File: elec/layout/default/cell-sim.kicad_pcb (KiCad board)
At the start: 2 copper layers, 225.7 x 100.8 mm, 0 parts

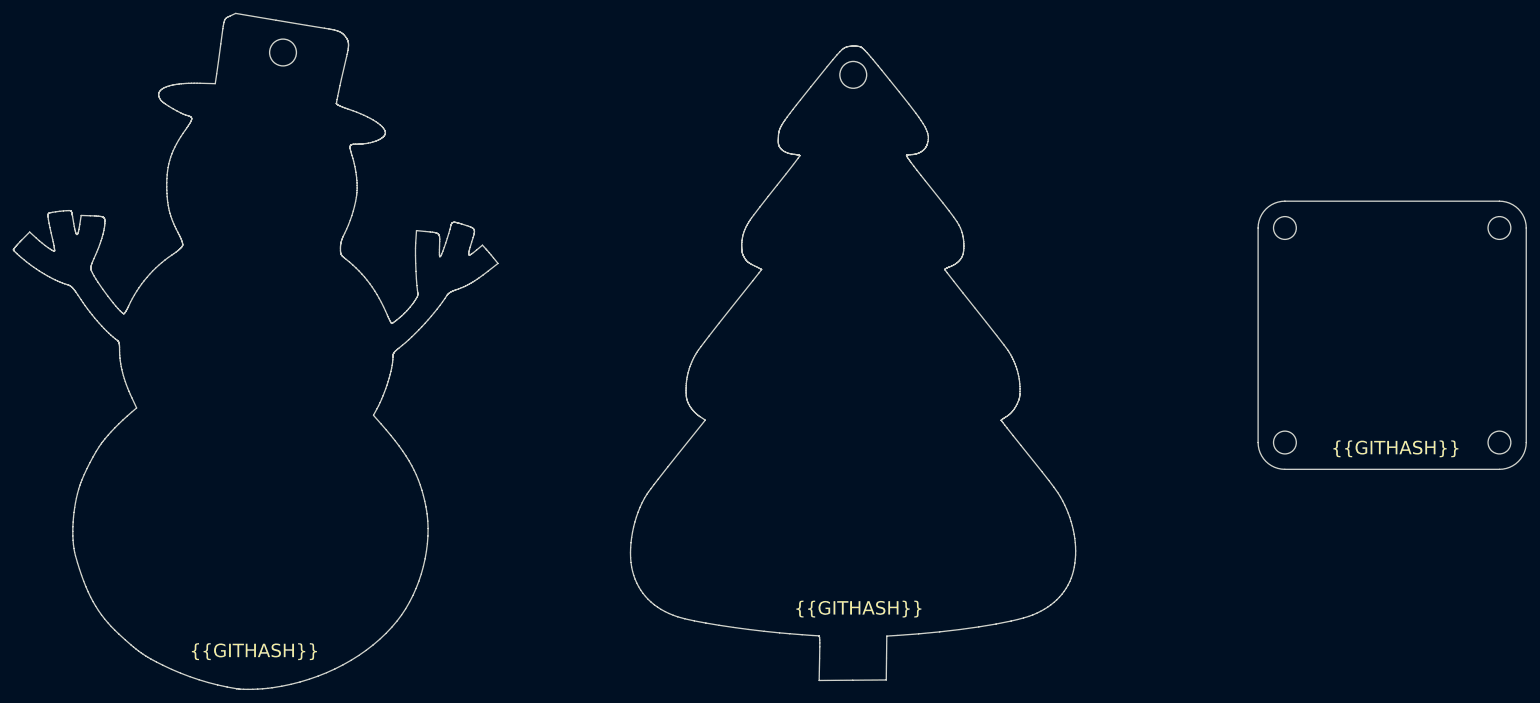
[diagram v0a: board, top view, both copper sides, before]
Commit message: merge firmware and layout from BMS project
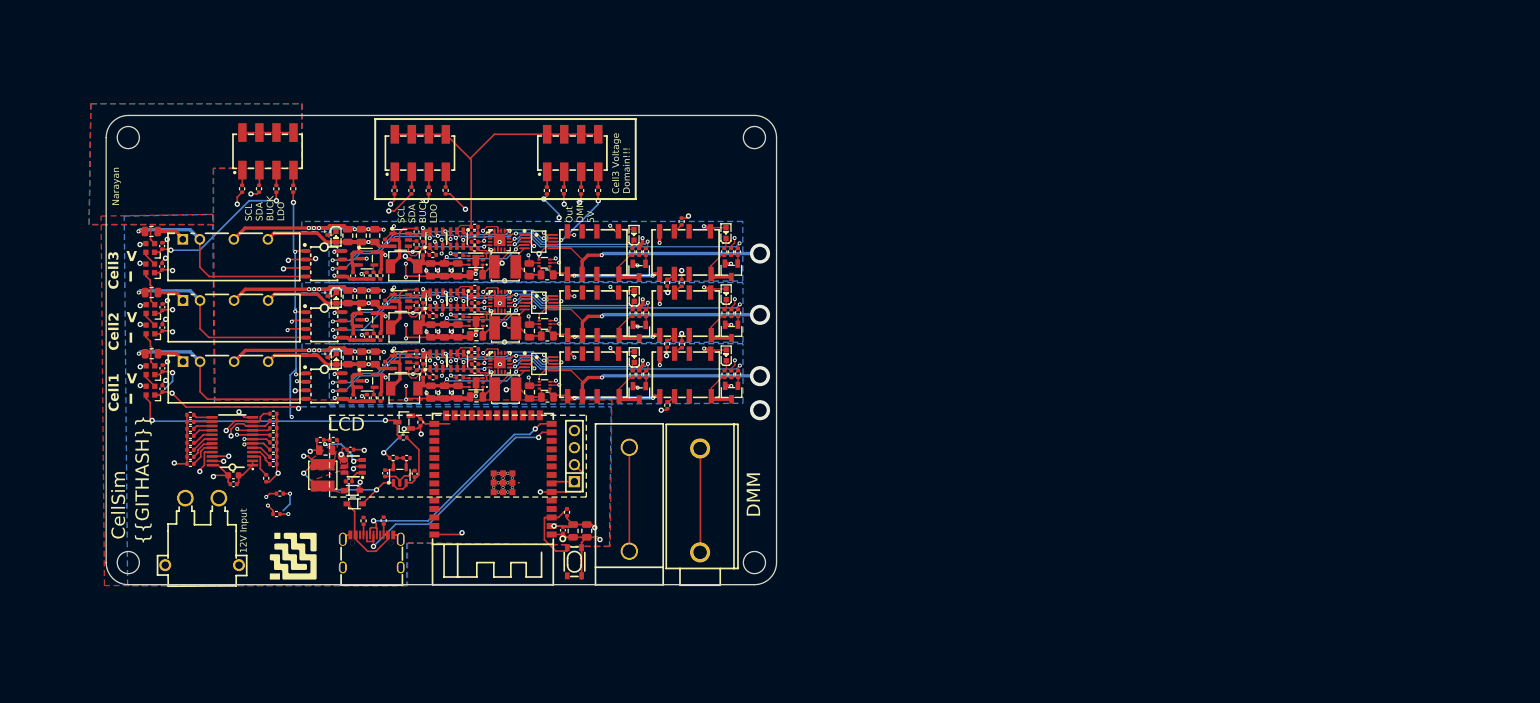
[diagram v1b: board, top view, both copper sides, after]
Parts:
- added C1: 16V 100nF X7R ±10% 0402 Multilayer Ceramic Capacitors MLCC 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, lib:C0402, F.Cu at (117.9, 126.9)
- added C10: 25V 1uF X5R ±10% 0402 Multilayer Ceramic Capacitors MLCC - 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, lib:C0402, F.Cu at (91.4, 118.4)
- added C11: 50V 2.2uF X5R ±10% 0805 Multilayer Ceramic Capacitors MLCC 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, lib:C0805, F.Cu at (56.6, 100.5)
- added C12: 25V 10uF X5R ±10% 0805 Multilayer Ceramic Capacitors MLCC -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, lib:C0805, F.Cu at (85.9, 101.2)
- added C13: 25V 10uF X5R ±10% 0805 Multilayer Ceramic Capacitors MLCC -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, lib:C0805, F.Cu at (89.9, 101.2)
- added C14: 25V 10uF X5R ±10% 0805 Multilayer Ceramic Capacitors MLCC -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, lib:C0805, F.Cu at (87.9, 101.2)
- added C15: 16V 100nF X7R ±10% 0402 Multilayer Ceramic Capacitors MLCC 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, lib:C0402, F.Cu at (91.4, 102.2)
- added C16: 25V 10uF X5R ±10% 0805 Multilayer Ceramic Capacitors MLCC -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, lib:C0805, F.Cu at (100.3, 106.3)
- added C17: 25V 10uF X5R ±10% 0805 Multilayer Ceramic Capacitors MLCC -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, lib:C0805, F.Cu at (102.3, 106.3)
- added C18: 25V 10uF X5R ±10% 0805 Multilayer Ceramic Capacitors MLCC -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, lib:C0805, F.Cu at (98.2, 106.3)
- added C19: 16V 100nF X7R ±10% 0402 Multilayer Ceramic Capacitors MLCC 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, lib:C0402, F.Cu at (96.1, 100.6)
- added C2: 25V 10uF X5R ±10% 0805 Multilayer Ceramic Capacitors MLCC -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, lib:C0805, F.Cu at (119.4, 127.0)
- added C20: 25V 1uF X5R ±10% 0402 Multilayer Ceramic Capacitors MLCC - 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, lib:C0402, F.Cu at (104.8, 102.1)
- added C21: 25V 10uF X5R ±10% 0805 Multilayer Ceramic Capacitors MLCC -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, lib:C0805, F.Cu at (105.0, 107.0)
- added C22: 25V 10uF X5R ±10% 0805 Multilayer Ceramic Capacitors MLCC -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, lib:C0805, F.Cu at (112.9, 106.3)
- added C23: 16V 100nF X7R ±10% 0402 Multilayer Ceramic Capacitors MLCC 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, lib:C0402, F.Cu at (58.2, 102.7)
- added C24: 16V 100nF X7R ±10% 0402 Multilayer Ceramic Capacitors MLCC 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, lib:C0402, F.Cu at (58.2, 105.8)
- added C25: 25V 1uF X5R ±10% 0402 Multilayer Ceramic Capacitors MLCC - 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, lib:C0402, F.Cu at (86.7, 107.1)
- added C26: 25V 1uF X5R ±10% 0402 Multilayer Ceramic Capacitors MLCC - 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, lib:C0402, F.Cu at (88.7, 107.1)
- added C27: 50V 2.2uF X5R ±10% 0805 Multilayer Ceramic Capacitors MLCC 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, lib:C0805, F.Cu at (56.6, 91.4)
- added C28: 25V 10uF X5R ±10% 0805 Multilayer Ceramic Capacitors MLCC -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, lib:C0805, F.Cu at (85.9, 92.0)
- added C29: 25V 10uF X5R ±10% 0805 Multilayer Ceramic Capacitors MLCC -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, lib:C0805, F.Cu at (89.9, 92.0)
- added C3: 25V 10uF X5R ±10% 0805 Multilayer Ceramic Capacitors MLCC -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, lib:C0805, F.Cu at (121.5, 127.0)
- added C30: 25V 10uF X5R ±10% 0805 Multilayer Ceramic Capacitors MLCC -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, lib:C0805, F.Cu at (87.9, 92.1)
- added C31: 16V 100nF X7R ±10% 0402 Multilayer Ceramic Capacitors MLCC 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, lib:C0402, F.Cu at (91.4, 93.1)
- added C32: 25V 10uF X5R ±10% 0805 Multilayer Ceramic Capacitors MLCC -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, lib:C0805, F.Cu at (100.3, 97.2)
- added C33: 25V 10uF X5R ±10% 0805 Multilayer Ceramic Capacitors MLCC -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, lib:C0805, F.Cu at (102.3, 97.2)
- added C34: 25V 10uF X5R ±10% 0805 Multilayer Ceramic Capacitors MLCC -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, lib:C0805, F.Cu at (98.2, 97.2)
- added C35: 16V 100nF X7R ±10% 0402 Multilayer Ceramic Capacitors MLCC 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, lib:C0402, F.Cu at (96.1, 91.5)
- added C36: 25V 1uF X5R ±10% 0402 Multilayer Ceramic Capacitors MLCC - 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, lib:C0402, F.Cu at (104.8, 93.0)
- added C37: 25V 10uF X5R ±10% 0805 Multilayer Ceramic Capacitors MLCC -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, lib:C0805, F.Cu at (105.0, 97.9)
- added C38: 25V 10uF X5R ±10% 0805 Multilayer Ceramic Capacitors MLCC -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, lib:C0805, F.Cu at (112.9, 97.2)
- added C39: 16V 100nF X7R ±10% 0402 Multilayer Ceramic Capacitors MLCC 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, lib:C0402, F.Cu at (58.2, 93.6)
- added C4: 16V 100nF X7R ±10% 0402 Multilayer Ceramic Capacitors MLCC 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, lib:C0402, F.Cu at (68.8, 120.0)
- added C40: 16V 100nF X7R ±10% 0402 Multilayer Ceramic Capacitors MLCC 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, lib:C0402, F.Cu at (58.2, 96.6)
- added C41: 25V 1uF X5R ±10% 0402 Multilayer Ceramic Capacitors MLCC - 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, lib:C0402, F.Cu at (86.6, 98.0)
- added C42: 25V 1uF X5R ±10% 0402 Multilayer Ceramic Capacitors MLCC - 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, lib:C0402, F.Cu at (88.7, 98.0)
- added C43: 50V 2.2uF X5R ±10% 0805 Multilayer Ceramic Capacitors MLCC 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, lib:C0805, F.Cu at (56.5, 82.3)
- added C44: 25V 10uF X5R ±10% 0805 Multilayer Ceramic Capacitors MLCC -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, lib:C0805, F.Cu at (85.8, 82.9)
- added C45: 25V 10uF X5R ±10% 0805 Multilayer Ceramic Capacitors MLCC -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, lib:C0805, F.Cu at (89.9, 82.9)
- added C46: 25V 10uF X5R ±10% 0805 Multilayer Ceramic Capacitors MLCC -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, lib:C0805, F.Cu at (87.8, 82.9)
- added C47: 16V 100nF X7R ±10% 0402 Multilayer Ceramic Capacitors MLCC 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, lib:C0402, F.Cu at (91.4, 84.0)
- added C48: 25V 10uF X5R ±10% 0805 Multilayer Ceramic Capacitors MLCC -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, lib:C0805, F.Cu at (100.2, 88.0)
- added C49: 25V 10uF X5R ±10% 0805 Multilayer Ceramic Capacitors MLCC -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, lib:C0805, F.Cu at (102.2, 88.0)
- added C5: 16V 2.2uF X5R ±10% 0603 Multilayer Ceramic Capacitors MLCC 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, lib:C0603, F.Cu at (68.8, 118.7)
- added C50: 25V 10uF X5R ±10% 0805 Multilayer Ceramic Capacitors MLCC -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, lib:C0805, F.Cu at (98.2, 88.0)
- added C51: 16V 100nF X7R ±10% 0402 Multilayer Ceramic Capacitors MLCC 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, lib:C0402, F.Cu at (96.1, 82.3)
- added C52: 25V 1uF X5R ±10% 0402 Multilayer Ceramic Capacitors MLCC - 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, lib:C0402, F.Cu at (104.8, 83.8)
- added C53: 25V 10uF X5R ±10% 0805 Multilayer Ceramic Capacitors MLCC -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, lib:C0805, F.Cu at (105.0, 88.8)
- added C54: 25V 10uF X5R ±10% 0805 Multilayer Ceramic Capacitors MLCC -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, lib:C0805, F.Cu at (112.9, 88.0)
- added C55: 16V 100nF X7R ±10% 0402 Multilayer Ceramic Capacitors MLCC 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, lib:C0402, F.Cu at (58.1, 84.5)
- added C56: 16V 100nF X7R ±10% 0402 Multilayer Ceramic Capacitors MLCC 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, lib:C0402, F.Cu at (58.1, 87.5)
- added C57: 25V 1uF X5R ±10% 0402 Multilayer Ceramic Capacitors MLCC - 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, lib:C0402, F.Cu at (86.6, 88.9)
- added C58: 25V 1uF X5R ±10% 0402 Multilayer Ceramic Capacitors MLCC - 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, lib:C0402, F.Cu at (88.6, 88.9)
- added C6: 6.3V 10uF X5R ±20% 0402 Multilayer Ceramic Capacitors MLCC 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, lib:C0402, F.Cu at (86.2, 114.9)
- added C7: 25V 10uF X5R ±10% 0805 Multilayer Ceramic Capacitors MLCC -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, lib:C0805, F.Cu at (82.5, 114.9)
- added C8: 16V 100nF X7R ±10% 0402 Multilayer Ceramic Capacitors MLCC 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, lib:C0402, F.Cu at (86.0, 119.6)
- added C9: 25V 1uF X5R ±10% 0402 Multilayer Ceramic Capacitors MLCC - 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, lib:C0402, F.Cu at (95.8, 118.5)
- added DS1: , lib:SOD-323_L1.8-W1.3-LS2.5-RD, F.Cu at (86.4, 120.9)
- added DS2: , lib:SOD-323_L1.8-W1.3-LS2.5-RD, F.Cu at (86.9, 122.9)
- added J1: , lib:CONN-TH_XT30PW-M, F.Cu at (64.1, 127.1)
- added L1: , lib:IND-SMD_L4.0-W4.0, F.Cu at (82.1, 118.7)
- added L2: , lib:IND-SMD_L4.4-W4.2, F.Cu at (94.3, 105.7)
- added L3: 100uH, lib:IND-SMD_L4.0-W4.0, F.Cu at (109.3, 105.8)
- added L4: , lib:IND-SMD_L4.4-W4.2, F.Cu at (94.3, 96.6)
- added L5: 100uH, lib:IND-SMD_L4.0-W4.0, F.Cu at (109.3, 96.7)
- added L6: , lib:IND-SMD_L4.4-W4.2, F.Cu at (94.2, 87.5)
- added L7: 100uH, lib:IND-SMD_L4.0-W4.0, F.Cu at (109.3, 87.6)
- added LED1: , lib:LED0603-RD, F.Cu at (84.1, 101.3)
- added LED2: , lib:LED0603-RD, F.Cu at (128.6, 101.0)
- added LED3: , lib:LED0603-RD, F.Cu at (142.3, 100.8)
- added LED4: , lib:LED0603-RD, F.Cu at (84.1, 92.2)
- added LED5: , lib:LED0603-RD, F.Cu at (128.6, 91.9)
- added LED6: , lib:LED0603-RD, F.Cu at (142.3, 91.7)
- added LED7: , lib:LED0603-RD, F.Cu at (84.1, 83.1)
- added LED8: , lib:LED0603-RD, F.Cu at (128.5, 82.8)
- added LED9: , lib:LED0603-RD, F.Cu at (142.2, 82.5)
- added Q1: , lib:SOT-23-3_L2.9-W1.3-P1.90-LS2.4-BR, F.Cu at (129.3, 106.4)
- added Q2: , lib:SOT-23-3_L2.9-W1.3-P1.90-LS2.4-BR, F.Cu at (143.1, 106.3)
- added Q3: , lib:SOT-23-3_L2.9-W1.3-P1.90-LS2.4-BR, F.Cu at (129.3, 97.3)
- added Q4: , lib:SOT-23-3_L2.9-W1.3-P1.90-LS2.4-BR, F.Cu at (143.1, 97.2)
- added Q5: , lib:SOT-23-3_L2.9-W1.3-P1.90-LS2.4-BR, F.Cu at (129.3, 88.1)
- added Q6: , lib:SOT-23-3_L2.9-W1.3-P1.90-LS2.4-BR, F.Cu at (143.0, 88.1)
- added R1: 62.5mW Thick Film Resistors 50V ±100ppm/℃ ±1% 10kΩ 0402 Chi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, lib:R0402, F.Cu at (118.5, 124.2)
- added R10: 62.5mW Thick Film Resistors 50V ±100ppm/℃ ±1% 10kΩ 0402 Chi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, lib:R0402, F.Cu at (74.7, 112.7)
- added R100: 62.5mW Thick Film Resistors 50V ±100ppm/℃ ±1% 1kΩ 0402 Chip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, lib:R0402, F.Cu at (123.2, 76.2)
- added R11: 62.5mW Thick Film Resistors 50V ±100ppm/℃ ±1% 10kΩ 0402 Chi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, lib:R0402, F.Cu at (74.7, 109.5)
- added R12: 62.5mW Thick Film Resistors 50V ±100ppm/℃ ±1% 10kΩ 0402 Chi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, lib:R0402, F.Cu at (74.7, 110.6)
- added R13: 62.5mW Thick Film Resistors 50V ±100ppm/℃ ±1% 10kΩ 0402 Chi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, lib:R0402, F.Cu at (62.3, 110.7)
- added R14: 62.5mW Thick Film Resistors 50V ±100ppm/℃ ±1% 10kΩ 0402 Chi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, lib:R0402, F.Cu at (62.3, 109.7)
- added R15: 62.5mW Thick Film Resistors 50V ±100ppm/℃ ±1% 10kΩ 0402 Chi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, lib:R0402, F.Cu at (62.3, 112.8)
- added R16: 62.5mW Thick Film Resistors 50V ±100ppm/℃ ±1% 10kΩ 0402 Chi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, lib:R0402, F.Cu at (62.3, 111.8)
- added R17: 62.5mW Thick Film Resistors 50V ±100ppm/℃ ±1% 10kΩ 0402 Chi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, lib:R0402, F.Cu at (62.3, 114.9)
- added R18: 62.5mW Thick Film Resistors 50V ±100ppm/℃ ±1% 10kΩ 0402 Chi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, lib:R0402, F.Cu at (62.3, 113.8)
- added R19: 62.5mW Thick Film Resistors 50V ±100ppm/℃ ±1% 10kΩ 0402 Chi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, lib:R0402, F.Cu at (62.3, 117.0)
- added R2: 62.5mW Thick Film Resistors 50V ±100ppm/℃ ±1% 4.7kΩ 0402 Ch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, lib:R0402, F.Cu at (88.2, 125.5)
- added R20: 62.5mW Thick Film Resistors 50V ±100ppm/℃ ±1% 10kΩ 0402 Chi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, lib:R0402, F.Cu at (62.3, 115.9)
- added R21: 62.5mW Thick Film Resistors 50V ±100ppm/℃ ±1% 2.2kΩ 0402 Ch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, lib:R0402, F.Cu at (75.2, 124.5)
- added R22: 62.5mW Thick Film Resistors 50V ±100ppm/℃ ±1% 2.2kΩ 0402 Ch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, lib:R0402, F.Cu at (75.7, 121.4)
- added R23: 62.5mW Thick Film Resistors 50V ±1% ±200ppm/℃ 22.6kΩ 0402 C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, lib:R0402, F.Cu at (83.7, 113.4)
- added R24: 62.5mW Thick Film Resistors 50V ±1% ±100ppm/℃ 4.12kΩ 0402 C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, lib:R0402, F.Cu at (81.7, 113.4)
- added R25: 62.5mW Thick Film Resistors 50V ±100ppm/℃ ±1% 17.4kΩ 0402 C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, lib:R0402, F.Cu at (92.6, 116.1)
- added R26: 62.5mW Thick Film Resistors 50V ±100ppm/℃ ±1% 10.2kΩ 0402 C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, lib:R0402, F.Cu at (94.6, 116.1)
- added R27: 62.5mW Thick Film Resistors 50V ±100ppm/℃ ±1% 10kΩ 0402 Chi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, lib:R0402, F.Cu at (96.7, 110.8)
- added R28: 62.5mW Thick Film Resistors 50V ±100ppm/℃ ±1% 10kΩ 0402 Chi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, lib:R0402, F.Cu at (94.1, 113.0)
- added R29: 62.5mW Thick Film Resistors 50V ±100ppm/℃ ±1% 21kΩ 0402 Chi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, lib:R0402, F.Cu at (82.8, 100.6)
- added R3: 62.5mW Thick Film Resistors 50V ±100ppm/℃ ±1% 4.7kΩ 0402 Ch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, lib:R0402, F.Cu at (91.2, 125.4)
- added R30: 62.5mW Thick Film Resistors 50V ±100ppm/℃ ±1% 24kΩ 0402 Chi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, lib:R0402, F.Cu at (98.5, 104.0)
- added R31: 62.5mW Thick Film Resistors 50V ±100ppm/℃ ±1% 37.4kΩ 0402 C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, lib:R0402, F.Cu at (97.1, 103.6)
- added R32: 62.5mW Thick Film Resistors 50V ±100ppm/℃ ±1% 10kΩ 0402 Chi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, lib:R0402, F.Cu at (97.1, 101.5)
- added R33: 62.5mW Thick Film Resistors 50V ±100ppm/℃ ±1% 10kΩ 0402 Chi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, lib:R0402, F.Cu at (96.1, 102.5)
- added R34: 62.5mW Thick Film Resistors 50V ±100ppm/℃ ±1% 43kΩ 0402 Chi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, lib:R0402, F.Cu at (104.8, 100.9)
- added R35: 62.5mW Thick Film Resistors 50V ±100ppm/℃ ±1% 59kΩ 0402 Chi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, lib:R0402, F.Cu at (104.8, 103.1)
- added R36: 62.5mW Thick Film Resistors 50V ±100ppm/℃ ±1% 10kΩ 0402 Chi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, lib:R0402, F.Cu at (104.8, 99.9)
- added R37: 62.5mW Thick Film Resistors 50V ±100ppm/℃ ±1% 10kΩ 0402 Chi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, lib:R0402, F.Cu at (102.5, 104.1)
- added R38: 125mW Thick Film Resistors ±600ppm/℃ ±1% 110mΩ 0805 Chip Re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, lib:R0805, F.Cu at (115.6, 107.0)
- added R39: 62.5mW Thick Film Resistors 50V ±100ppm/℃ ±1% 21kΩ 0402 Chi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, lib:R0402, F.Cu at (128.3, 103.6)
- added R4: 62.5mW Thick Film Resistors 50V ±100ppm/℃ ±1% 10kΩ 0402 Chi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, lib:R0402, F.Cu at (73.7, 119.1)
- added R40: 62.5mW Thick Film Resistors 50V ±100ppm/℃ ±1% 10kΩ 0402 Chi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, lib:R0402, F.Cu at (130.3, 103.6)
- added R41: 62.5mW Thick Film Resistors 50V ±100ppm/℃ ±1% 1kΩ 0402 Chip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, lib:R0402, F.Cu at (129.3, 103.6)
- added R42: 62.5mW Thick Film Resistors 50V ±100ppm/℃ ±1% 21kΩ 0402 Chi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, lib:R0402, F.Cu at (142.0, 103.6)
- added R43: 62.5mW Thick Film Resistors 50V ±100ppm/℃ ±1% 10kΩ 0402 Chi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, lib:R0402, F.Cu at (144.1, 103.6)
- added R44: 62.5mW Thick Film Resistors 50V ±100ppm/℃ ±1% 1kΩ 0402 Chip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, lib:R0402, F.Cu at (143.0, 103.6)
- added R45: 62.5mW Thick Film Resistors 50V ±100ppm/℃ ±1% 11.5kΩ 0402 C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, lib:R0402, F.Cu at (90.7, 107.1)
- added R46: 62.5mW Thick Film Resistors 50V ±100ppm/℃ ±1% 6.2kΩ 0402 Ch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, lib:R0402, F.Cu at (89.7, 107.1)
- added R47: 62.5mW Thick Film Resistors 50V ±100ppm/℃ ±1% 10kΩ 0402 Chi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, lib:R0402, F.Cu at (133.5, 108.2)
- added R48: 62.5mW Thick Film Resistors 50V ±100ppm/℃ ±1% 10kΩ 0402 Chi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, lib:R0402, F.Cu at (135.7, 99.1)
- added R49: 62.5mW Thick Film Resistors 50V ±100ppm/℃ ±1% 21kΩ 0402 Chi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, lib:R0402, F.Cu at (82.8, 91.4)
- added R5: 62.5mW Thick Film Resistors 50V ±100ppm/℃ ±1% 10kΩ 0402 Chi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, lib:R0402, F.Cu at (74.7, 115.9)
- added R50: 62.5mW Thick Film Resistors 50V ±100ppm/℃ ±1% 24kΩ 0402 Chi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, lib:R0402, F.Cu at (98.5, 94.9)
- added R51: 62.5mW Thick Film Resistors 50V ±100ppm/℃ ±1% 37.4kΩ 0402 C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, lib:R0402, F.Cu at (97.1, 94.5)
- added R52: 62.5mW Thick Film Resistors 50V ±100ppm/℃ ±1% 10kΩ 0402 Chi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, lib:R0402, F.Cu at (97.1, 92.4)
- added R53: 62.5mW Thick Film Resistors 50V ±100ppm/℃ ±1% 10kΩ 0402 Chi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, lib:R0402, F.Cu at (96.1, 93.4)
- added R54: 62.5mW Thick Film Resistors 50V ±100ppm/℃ ±1% 43kΩ 0402 Chi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, lib:R0402, F.Cu at (104.8, 91.8)
- added R55: 62.5mW Thick Film Resistors 50V ±100ppm/℃ ±1% 59kΩ 0402 Chi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, lib:R0402, F.Cu at (104.8, 94.0)
- added R56: 62.5mW Thick Film Resistors 50V ±100ppm/℃ ±1% 10kΩ 0402 Chi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, lib:R0402, F.Cu at (104.8, 90.7)
- added R57: 62.5mW Thick Film Resistors 50V ±100ppm/℃ ±1% 10kΩ 0402 Chi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, lib:R0402, F.Cu at (102.5, 95.0)
- added R58: 125mW Thick Film Resistors ±600ppm/℃ ±1% 110mΩ 0805 Chip Re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, lib:R0805, F.Cu at (115.6, 97.9)
- added R59: 62.5mW Thick Film Resistors 50V ±100ppm/℃ ±1% 21kΩ 0402 Chi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, lib:R0402, F.Cu at (128.3, 94.5)
- added R6: 62.5mW Thick Film Resistors 50V ±100ppm/℃ ±1% 10kΩ 0402 Chi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, lib:R0402, F.Cu at (74.7, 117.0)
- added R60: 62.5mW Thick Film Resistors 50V ±100ppm/℃ ±1% 10kΩ 0402 Chi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, lib:R0402, F.Cu at (130.3, 94.5)
- added R61: 62.5mW Thick Film Resistors 50V ±100ppm/℃ ±1% 1kΩ 0402 Chip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, lib:R0402, F.Cu at (129.3, 94.5)
- added R62: 62.5mW Thick Film Resistors 50V ±100ppm/℃ ±1% 21kΩ 0402 Chi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, lib:R0402, F.Cu at (142.0, 94.5)
- added R63: 62.5mW Thick Film Resistors 50V ±100ppm/℃ ±1% 10kΩ 0402 Chi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, lib:R0402, F.Cu at (144.1, 94.5)
- added R64: 62.5mW Thick Film Resistors 50V ±100ppm/℃ ±1% 1kΩ 0402 Chip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, lib:R0402, F.Cu at (143.0, 94.5)
- added R65: 62.5mW Thick Film Resistors 50V ±100ppm/℃ ±1% 11.5kΩ 0402 C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, lib:R0402, F.Cu at (90.7, 98.0)
- added R66: 62.5mW Thick Film Resistors 50V ±100ppm/℃ ±1% 6.2kΩ 0402 Ch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, lib:R0402, F.Cu at (89.7, 98.0)
- added R67: 62.5mW Thick Film Resistors 50V ±100ppm/℃ ±1% 10kΩ 0402 Chi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, lib:R0402, F.Cu at (133.5, 99.1)
- added R68: 62.5mW Thick Film Resistors 50V ±100ppm/℃ ±1% 10kΩ 0402 Chi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, lib:R0402, F.Cu at (135.6, 90.0)
- added R69: 62.5mW Thick Film Resistors 50V ±100ppm/℃ ±1% 21kΩ 0402 Chi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, lib:R0402, F.Cu at (82.8, 82.3)
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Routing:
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- added copper zone on F.Cu, net buck.ic-sw
- added copper zone on B.Cu, net cell1-gnd
- added copper zone on In2.Cu, net cell1-gnd
- added copper zone on In1.Cu, net cell1-vcc-2
- added copper zone on B.Cu, net cell2-gnd-1
- added copper zone on In2.Cu, net cell2-gnd-1
- added copper zone on In1.Cu, net cell2-vcc-2
- added copper zone on In1.Cu, net cell3-vcc-2
- added copper zone on B.Cu, net gnd
- added copper zone on F.Cu, net gnd
- added copper zone on In2.Cu, net gnd
- added copper zone on F.Cu, net vcc
- added copper zone on F.Cu, net vcc-2
- added copper zone on B.Cu, net vcc-3
- added copper zone on In1.Cu, net vcc-3
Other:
- board size 225.7 x 100.8 mm -> 100 x 70 mm
- copper layers 2 -> 4
- board text added: "12V Input"
- board text added: "Cell1"
- board text added: "Cell2"
- board text added: "Cell3"
- board text added: "Cell3 Voltage Domain!!!"
- board text added: "CellSim"
- board text added: "DMM"
- board text added: "I"
- board text added: "I Out DMM 5V"
- board text added: "LCD"
- board text added: "Narayan"
- board text added: "SCL SDA BUCK LDO"
- board text added: "V"

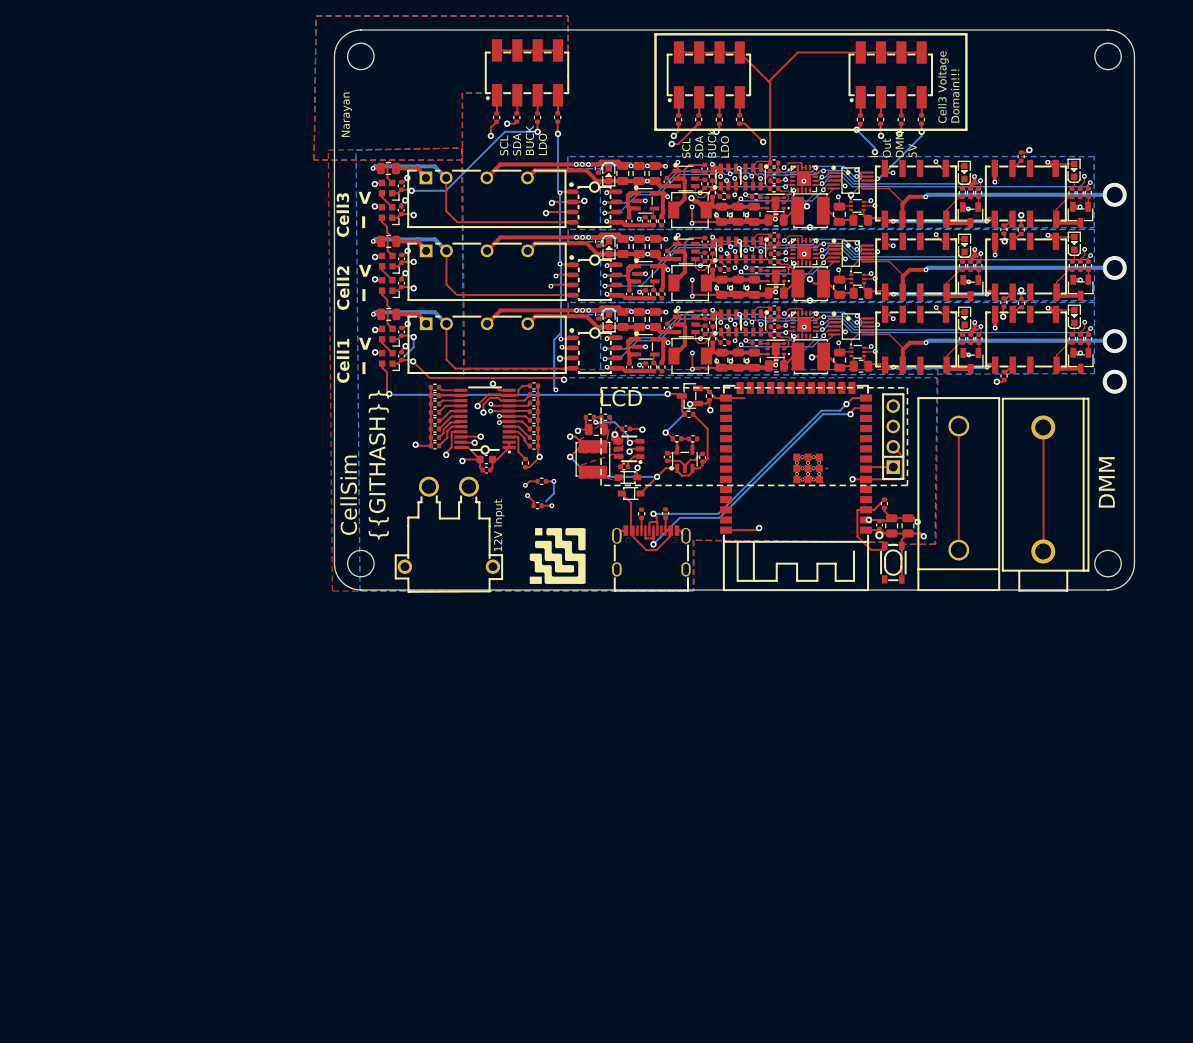
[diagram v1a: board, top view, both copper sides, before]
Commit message: add library parts
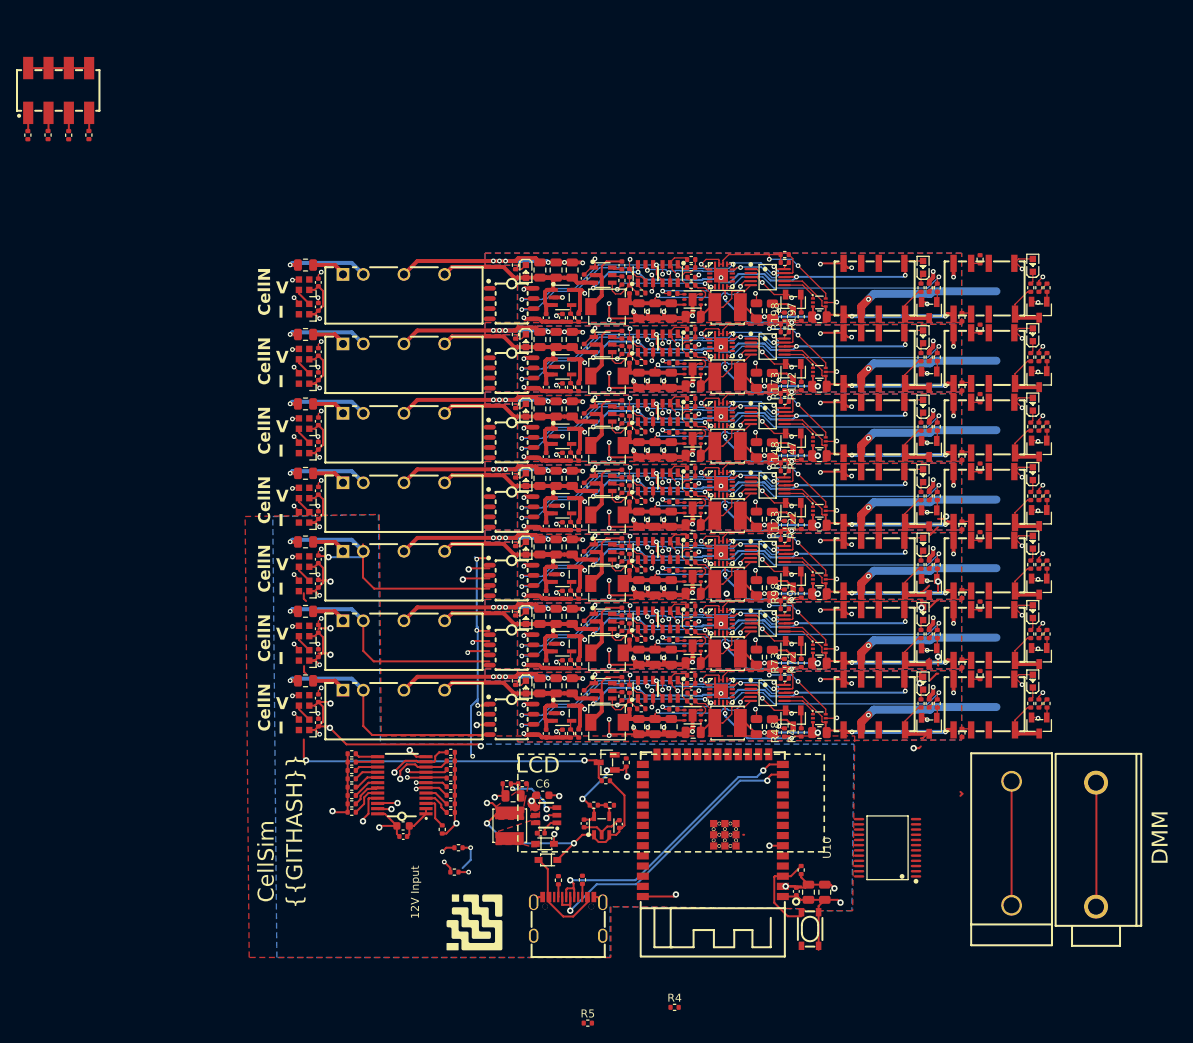
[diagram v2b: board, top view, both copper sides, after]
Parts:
- removed J1: , lib:CONN-TH_XT30PW-M
- removed the R93 at (92.8, 76.2)
- removed the R94 at (95.3, 76.2)
- removed the R95 at (97.9, 76.2)
- removed the R96 at (100.4, 76.2)
- removed the U6 at (119.6, 115.8)
- added C100: 25V 1uF X5R ±10% 0402 Multilayer Ceramic Capacitors MLCC - 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, lib:C0402, F.Cu at (94.4, 104.6)
- added C101: 25V 10uF X5R ±10% 0805 Multilayer Ceramic Capacitors MLCC -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, lib:C0805, F.Cu at (94.6, 109.5)
- added C102: 25V 10uF X5R ±10% 0805 Multilayer Ceramic Capacitors MLCC -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, lib:C0805, F.Cu at (102.5, 108.8)
- added C103: 16V 100nF X7R ±10% 0402 Multilayer Ceramic Capacitors MLCC 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, lib:C0402, F.Cu at (47.8, 105.2)
- added C104: 16V 100nF X7R ±10% 0402 Multilayer Ceramic Capacitors MLCC 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, lib:C0402, F.Cu at (47.8, 108.3)
- added C105: 25V 1uF X5R ±10% 0402 Multilayer Ceramic Capacitors MLCC - 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, lib:C0402, F.Cu at (76.3, 109.6)
- added C106: 25V 1uF X5R ±10% 0402 Multilayer Ceramic Capacitors MLCC - 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, lib:C0402, F.Cu at (78.3, 109.6)
- added C107: 50V 2.2uF X5R ±10% 0805 Multilayer Ceramic Capacitors MLCC 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, lib:C0805, F.Cu at (46.2, 94.4)
- added C108: 25V 10uF X5R ±10% 0805 Multilayer Ceramic Capacitors MLCC -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, lib:C0805, F.Cu at (75.5, 95.0)
- added C109: 25V 10uF X5R ±10% 0805 Multilayer Ceramic Capacitors MLCC -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, lib:C0805, F.Cu at (79.5, 95.0)
- added C110: 25V 10uF X5R ±10% 0805 Multilayer Ceramic Capacitors MLCC -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, lib:C0805, F.Cu at (77.5, 95.0)
- added C111: 16V 100nF X7R ±10% 0402 Multilayer Ceramic Capacitors MLCC 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, lib:C0402, F.Cu at (81.0, 96.0)
- added C112: 25V 10uF X5R ±10% 0805 Multilayer Ceramic Capacitors MLCC -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, lib:C0805, F.Cu at (89.9, 100.1)
- added C113: 25V 10uF X5R ±10% 0805 Multilayer Ceramic Capacitors MLCC -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, lib:C0805, F.Cu at (91.9, 100.1)
- added C114: 25V 10uF X5R ±10% 0805 Multilayer Ceramic Capacitors MLCC -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, lib:C0805, F.Cu at (87.8, 100.1)
- added C115: 16V 100nF X7R ±10% 0402 Multilayer Ceramic Capacitors MLCC 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, lib:C0402, F.Cu at (85.7, 94.4)
- added C116: 25V 1uF X5R ±10% 0402 Multilayer Ceramic Capacitors MLCC - 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, lib:C0402, F.Cu at (94.4, 95.9)
- added C117: 25V 10uF X5R ±10% 0805 Multilayer Ceramic Capacitors MLCC -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, lib:C0805, F.Cu at (94.6, 100.8)
- added C118: 25V 10uF X5R ±10% 0805 Multilayer Ceramic Capacitors MLCC -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, lib:C0805, F.Cu at (102.5, 100.1)
- added C119: 16V 100nF X7R ±10% 0402 Multilayer Ceramic Capacitors MLCC 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, lib:C0402, F.Cu at (47.8, 96.5)
- added C120: 16V 100nF X7R ±10% 0402 Multilayer Ceramic Capacitors MLCC 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, lib:C0402, F.Cu at (47.8, 99.6)
- added C121: 25V 1uF X5R ±10% 0402 Multilayer Ceramic Capacitors MLCC - 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, lib:C0402, F.Cu at (76.3, 101.0)
- added C122: 25V 1uF X5R ±10% 0402 Multilayer Ceramic Capacitors MLCC - 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, lib:C0402, F.Cu at (78.3, 101.0)
- added C59: 50V 2.2uF X5R ±10% 0805 Multilayer Ceramic Capacitors MLCC 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, lib:C0805, F.Cu at (46.2, 120.4)
- added C60: 25V 10uF X5R ±10% 0805 Multilayer Ceramic Capacitors MLCC -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, lib:C0805, F.Cu at (75.5, 121.0)
- added C61: 25V 10uF X5R ±10% 0805 Multilayer Ceramic Capacitors MLCC -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, lib:C0805, F.Cu at (79.5, 121.0)
- added C62: 25V 10uF X5R ±10% 0805 Multilayer Ceramic Capacitors MLCC -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, lib:C0805, F.Cu at (77.5, 121.0)
- added C63: 16V 100nF X7R ±10% 0402 Multilayer Ceramic Capacitors MLCC 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, lib:C0402, F.Cu at (81.0, 122.1)
- added C64: 25V 10uF X5R ±10% 0805 Multilayer Ceramic Capacitors MLCC -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, lib:C0805, F.Cu at (89.9, 126.1)
- added C65: 25V 10uF X5R ±10% 0805 Multilayer Ceramic Capacitors MLCC -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, lib:C0805, F.Cu at (91.9, 126.1)
- added C66: 25V 10uF X5R ±10% 0805 Multilayer Ceramic Capacitors MLCC -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, lib:C0805, F.Cu at (87.8, 126.1)
- added C67: 16V 100nF X7R ±10% 0402 Multilayer Ceramic Capacitors MLCC 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, lib:C0402, F.Cu at (85.7, 120.4)
- added C68: 25V 1uF X5R ±10% 0402 Multilayer Ceramic Capacitors MLCC - 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, lib:C0402, F.Cu at (94.4, 121.9)
- added C69: 25V 10uF X5R ±10% 0805 Multilayer Ceramic Capacitors MLCC -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, lib:C0805, F.Cu at (94.6, 126.9)
- added C70: 25V 10uF X5R ±10% 0805 Multilayer Ceramic Capacitors MLCC -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, lib:C0805, F.Cu at (102.5, 126.1)
- added C71: 16V 100nF X7R ±10% 0402 Multilayer Ceramic Capacitors MLCC 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, lib:C0402, F.Cu at (47.8, 122.6)
- added C72: 16V 100nF X7R ±10% 0402 Multilayer Ceramic Capacitors MLCC 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, lib:C0402, F.Cu at (47.8, 125.6)
- added C73: 25V 1uF X5R ±10% 0402 Multilayer Ceramic Capacitors MLCC - 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, lib:C0402, F.Cu at (76.3, 127.0)
- added C74: 25V 1uF X5R ±10% 0402 Multilayer Ceramic Capacitors MLCC - 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, lib:C0402, F.Cu at (78.3, 127.0)
- added C75: 50V 2.2uF X5R ±10% 0805 Multilayer Ceramic Capacitors MLCC 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, lib:C0805, F.Cu at (46.2, 111.7)
- added C76: 25V 10uF X5R ±10% 0805 Multilayer Ceramic Capacitors MLCC -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, lib:C0805, F.Cu at (75.5, 112.4)
- added C77: 25V 10uF X5R ±10% 0805 Multilayer Ceramic Capacitors MLCC -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, lib:C0805, F.Cu at (79.5, 112.4)
- added C78: 25V 10uF X5R ±10% 0805 Multilayer Ceramic Capacitors MLCC -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, lib:C0805, F.Cu at (77.5, 112.4)
- added C79: 16V 100nF X7R ±10% 0402 Multilayer Ceramic Capacitors MLCC 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, lib:C0402, F.Cu at (81.0, 113.4)
- added C80: 25V 10uF X5R ±10% 0805 Multilayer Ceramic Capacitors MLCC -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, lib:C0805, F.Cu at (89.9, 117.5)
- added C81: 25V 10uF X5R ±10% 0805 Multilayer Ceramic Capacitors MLCC -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, lib:C0805, F.Cu at (91.9, 117.5)
- added C82: 25V 10uF X5R ±10% 0805 Multilayer Ceramic Capacitors MLCC -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, lib:C0805, F.Cu at (87.8, 117.5)
- added C83: 16V 100nF X7R ±10% 0402 Multilayer Ceramic Capacitors MLCC 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, lib:C0402, F.Cu at (85.7, 111.8)
- added C84: 25V 1uF X5R ±10% 0402 Multilayer Ceramic Capacitors MLCC - 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, lib:C0402, F.Cu at (94.4, 113.3)
- added C85: 25V 10uF X5R ±10% 0805 Multilayer Ceramic Capacitors MLCC -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, lib:C0805, F.Cu at (94.6, 118.2)
- added C86: 25V 10uF X5R ±10% 0805 Multilayer Ceramic Capacitors MLCC -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, lib:C0805, F.Cu at (102.5, 117.5)
- added C87: 16V 100nF X7R ±10% 0402 Multilayer Ceramic Capacitors MLCC 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, lib:C0402, F.Cu at (47.8, 113.9)
- added C88: 16V 100nF X7R ±10% 0402 Multilayer Ceramic Capacitors MLCC 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, lib:C0402, F.Cu at (47.8, 117.0)
- added C89: 25V 1uF X5R ±10% 0402 Multilayer Ceramic Capacitors MLCC - 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, lib:C0402, F.Cu at (76.3, 118.3)
- added C90: 25V 1uF X5R ±10% 0402 Multilayer Ceramic Capacitors MLCC - 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, lib:C0402, F.Cu at (78.3, 118.3)
- added C91: 50V 2.2uF X5R ±10% 0805 Multilayer Ceramic Capacitors MLCC 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, lib:C0805, F.Cu at (46.2, 103.1)
- added C92: 25V 10uF X5R ±10% 0805 Multilayer Ceramic Capacitors MLCC -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, lib:C0805, F.Cu at (75.5, 103.7)
- added C93: 25V 10uF X5R ±10% 0805 Multilayer Ceramic Capacitors MLCC -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, lib:C0805, F.Cu at (79.5, 103.7)
- added C94: 25V 10uF X5R ±10% 0805 Multilayer Ceramic Capacitors MLCC -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, lib:C0805, F.Cu at (77.5, 103.7)
- added C95: 16V 100nF X7R ±10% 0402 Multilayer Ceramic Capacitors MLCC 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, lib:C0402, F.Cu at (81.0, 104.7)
- added C96: 25V 10uF X5R ±10% 0805 Multilayer Ceramic Capacitors MLCC -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, lib:C0805, F.Cu at (89.9, 108.8)
- added C97: 25V 10uF X5R ±10% 0805 Multilayer Ceramic Capacitors MLCC -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, lib:C0805, F.Cu at (91.9, 108.8)
- added C98: 25V 10uF X5R ±10% 0805 Multilayer Ceramic Capacitors MLCC -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, lib:C0805, F.Cu at (87.8, 108.8)
- added C99: 16V 100nF X7R ±10% 0402 Multilayer Ceramic Capacitors MLCC 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, lib:C0402, F.Cu at (85.7, 103.1)
- added L10: ?, lib:IND-SMD_L4.4-W4.2, F.Cu at (83.9, 116.9)
- added L11: ?, lib:IND-SMD_L4.0-W4.0, F.Cu at (98.9, 117.0)
- added L12: ?, lib:IND-SMD_L4.4-W4.2, F.Cu at (83.9, 108.3)
- added L13: ?, lib:IND-SMD_L4.0-W4.0, F.Cu at (98.9, 108.3)
- added L14: ?, lib:IND-SMD_L4.4-W4.2, F.Cu at (83.9, 99.6)
- added L15: ?, lib:IND-SMD_L4.0-W4.0, F.Cu at (98.9, 99.7)
- added L8: ?, lib:IND-SMD_L4.4-W4.2, F.Cu at (83.9, 125.6)
- added L9: ?, lib:IND-SMD_L4.0-W4.0, F.Cu at (98.9, 125.7)
- added LED10: ?, lib:LED0603-RD, F.Cu at (73.7, 121.2)
- added LED11: ?, lib:LED0603-RD, F.Cu at (123.4, 120.7)
- added LED12: ?, lib:LED0603-RD, F.Cu at (137.1, 120.5)
- added LED13: ?, lib:LED0603-RD, F.Cu at (73.7, 112.5)
- added LED14: ?, lib:LED0603-RD, F.Cu at (123.4, 112.0)
- added LED15: ?, lib:LED0603-RD, F.Cu at (137.1, 111.8)
- added LED16: ?, lib:LED0603-RD, F.Cu at (73.7, 103.8)
- added LED17: ?, lib:LED0603-RD, F.Cu at (123.4, 103.4)
- added LED18: ?, lib:LED0603-RD, F.Cu at (137.1, 103.1)
- added LED19: ?, lib:LED0603-RD, F.Cu at (73.7, 95.2)
- added LED20: ?, lib:LED0603-RD, F.Cu at (123.4, 94.7)
- added LED21: ?, lib:LED0603-RD, F.Cu at (137.1, 94.4)
- added Q10: ?, lib:SOT-23-3_L2.9-W1.3-P1.90-LS2.4-BR, F.Cu at (124.1, 126.0)
- added Q11: ?, lib:SOT-23-3_L2.9-W1.3-P1.90-LS2.4-BR, F.Cu at (137.9, 126.0)
- added Q12: ?, lib:SOT-23-3_L2.9-W1.3-P1.90-LS2.4-BR, F.Cu at (107.1, 125.1)
- added Q13: ?, lib:SOT-23-3_L2.9-W1.3-P1.90-LS2.4-BR, F.Cu at (124.1, 117.4)
- added Q14: ?, lib:SOT-23-3_L2.9-W1.3-P1.90-LS2.4-BR, F.Cu at (137.9, 117.3)
- added Q15: ?, lib:SOT-23-3_L2.9-W1.3-P1.90-LS2.4-BR, F.Cu at (107.1, 116.4)
- added Q16: ?, lib:SOT-23-3_L2.9-W1.3-P1.90-LS2.4-BR, F.Cu at (124.1, 108.7)
- added Q17: ?, lib:SOT-23-3_L2.9-W1.3-P1.90-LS2.4-BR, F.Cu at (137.9, 108.6)
- added Q18: ?, lib:SOT-23-3_L2.9-W1.3-P1.90-LS2.4-BR, F.Cu at (107.1, 107.7)
- added Q19: ?, lib:SOT-23-3_L2.9-W1.3-P1.90-LS2.4-BR, F.Cu at (124.1, 100.0)
- added Q20: ?, lib:SOT-23-3_L2.9-W1.3-P1.90-LS2.4-BR, F.Cu at (137.9, 100.0)
- added Q21: ?, lib:SOT-23-3_L2.9-W1.3-P1.90-LS2.4-BR, F.Cu at (107.1, 99.1)
- added Q3: ?, lib:SOT-23-3_L2.9-W1.3-P1.90-LS2.4-BR, F.Cu at (107.1, 151.0)
- added Q6: ?, lib:SOT-23-3_L2.9-W1.3-P1.90-LS2.4-BR, F.Cu at (107.1, 142.4)
- added Q9: ?, lib:SOT-23-3_L2.9-W1.3-P1.90-LS2.4-BR, F.Cu at (107.1, 133.7)
- added R101: 62.5mW Thick Film Resistors 50V ±100ppm/℃ ±1% 10kΩ 0402 Chi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, lib:R0402, F.Cu at (106.1, 128.7)
- added R106: 62.5mW Thick Film Resistors 50V ±100ppm/℃ ±1% 14kΩ 0402 Chi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, lib:R0402, F.Cu at (72.4, 120.4)
- added R107: 62.5mW Thick Film Resistors 50V ±100ppm/℃ ±1% 24kΩ 0402 Chi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, lib:R0402, F.Cu at (88.1, 123.9)
- added R108: 62.5mW Thick Film Resistors 50V ±100ppm/℃ ±1% 37.4kΩ 0402 C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, lib:R0402, F.Cu at (86.7, 123.5)
- added R109: 62.5mW Thick Film Resistors 50V ±100ppm/℃ ±1% 10kΩ 0402 Chi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, lib:R0402, F.Cu at (86.7, 121.4)
- added R110: 62.5mW Thick Film Resistors 50V ±100ppm/℃ ±1% 10kΩ 0402 Chi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, lib:R0402, F.Cu at (85.7, 122.3)
- added R111: 62.5mW Thick Film Resistors 50V ±100ppm/℃ ±1% 43kΩ 0402 Chi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, lib:R0402, F.Cu at (94.4, 120.7)
- added R112: 62.5mW Thick Film Resistors 50V ±100ppm/℃ ±1% 60.4kΩ 0402 C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, lib:R0402, F.Cu at (94.4, 122.9)
- added R113: 62.5mW Thick Film Resistors 50V ±100ppm/℃ ±1% 10kΩ 0402 Chi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, lib:R0402, F.Cu at (94.4, 119.7)
- added R114: 62.5mW Thick Film Resistors 50V ±100ppm/℃ ±1% 10kΩ 0402 Chi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, lib:R0402, F.Cu at (92.1, 124.0)
- added R115: 125mW Thick Film Resistors 150V ±1% 100mΩ 0805 Chip Resisto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, lib:R0805, F.Cu at (110.4, 126.9)
- added R116: 62.5mW Thick Film Resistors 50V ±100ppm/℃ ±1% 13kΩ 0402 Chi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, lib:R0402, F.Cu at (123.1, 123.3)
- added R117: 62.5mW Thick Film Resistors 50V ±100ppm/℃ ±1% 10kΩ 0402 Chi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, lib:R0402, F.Cu at (125.1, 123.3)
- added R118: 62.5mW Thick Film Resistors 50V ±100ppm/℃ ±1% 1kΩ 0402 Chip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, lib:R0402, F.Cu at (124.1, 123.3)
- added R119: 62.5mW Thick Film Resistors 50V ±100ppm/℃ ±1% 13kΩ 0402 Chi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, lib:R0402, F.Cu at (136.8, 123.3)
- added R120: 62.5mW Thick Film Resistors 50V ±100ppm/℃ ±1% 10kΩ 0402 Chi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, lib:R0402, F.Cu at (138.9, 123.3)
- added R121: 62.5mW Thick Film Resistors 50V ±100ppm/℃ ±1% 1kΩ 0402 Chip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, lib:R0402, F.Cu at (137.8, 123.3)
- added R122: 62.5mW Thick Film Resistors 50V ±100ppm/℃ ±1% 1kΩ 0402 Chip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, lib:R0402, F.Cu at (108.1, 126.9)
- added R123: 62.5mW Thick Film Resistors 50V ±100ppm/℃ ±1% 10kΩ 0402 Chi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, lib:R0402, F.Cu at (106.0, 126.9)
- added R124: 125mW Thick Film Resistors 150V ±100ppm/℃ ±1% 226Ω 0805 Chi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, lib:R0805, F.Cu at (104.5, 126.1)
- added R125: 62.5mW Thick Film Resistors 50V ±100ppm/℃ ±1% 10kΩ 0402 Chi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, lib:R0402, F.Cu at (106.1, 119.1)
- added R126: 62.5mW Thick Film Resistors 50V ±100ppm/℃ ±1% 10kΩ 0402 Chi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, lib:R0402, F.Cu at (106.1, 120.1)
- added R127: 62.5mW Thick Film Resistors 50V ±100ppm/℃ ±1% 11.5kΩ 0402 C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, lib:R0402, F.Cu at (80.3, 127.0)
- added R128: 62.5mW Thick Film Resistors 50V ±100ppm/℃ ±1% 6.2kΩ 0402 Ch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, lib:R0402, F.Cu at (79.3, 127.0)
- added R129: 62.5mW Thick Film Resistors 50V ±100ppm/℃ ±1% 10kΩ 0402 Chi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, lib:R0402, F.Cu at (128.2, 126.9)
- added R130: 62.5mW Thick Film Resistors 50V ±100ppm/℃ ±1% 10kΩ 0402 Chi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, lib:R0402, F.Cu at (130.5, 119.7)
- added R131: 62.5mW Thick Film Resistors 50V ±100ppm/℃ ±1% 14kΩ 0402 Chi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, lib:R0402, F.Cu at (72.4, 111.7)
- added R132: 62.5mW Thick Film Resistors 50V ±100ppm/℃ ±1% 24kΩ 0402 Chi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, lib:R0402, F.Cu at (88.1, 115.2)
- added R133: 62.5mW Thick Film Resistors 50V ±100ppm/℃ ±1% 37.4kΩ 0402 C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, lib:R0402, F.Cu at (86.7, 114.8)
- added R134: 62.5mW Thick Film Resistors 50V ±100ppm/℃ ±1% 10kΩ 0402 Chi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, lib:R0402, F.Cu at (86.7, 112.7)
- added R135: 62.5mW Thick Film Resistors 50V ±100ppm/℃ ±1% 10kΩ 0402 Chi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, lib:R0402, F.Cu at (85.7, 113.7)
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- renumbered R25 to R27
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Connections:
- net cell1.gpio-int_hash renamed cell1.gpio-int
- net cell2.gpio-int_hash renamed cell2.gpio-int
- net cell3.gpio-int_hash renamed cell3.gpio-int
- net i2c_debug.header-_1 renamed _1
- net i2c_debug.header-_3 renamed _3
- net i2c_debug.header-_5 renamed _5
- net i2c_debug.header-_7 renamed _7
- C22 pad 1: cell1-gnd -> cell1-gnd-1
- C28 pad 2: cell1-gnd -> cell1-gnd-1
- C29 pad 2: cell1-gnd -> cell1-gnd-1
- C30 pad 2: cell1-gnd -> cell1-gnd-1
- C31 pad 2: cell1-gnd -> cell1-gnd-1
- C32 pad 2: cell1-gnd -> cell1-gnd-1
- C33 pad 2: cell1-gnd -> cell1-gnd-1
- C34 pad 2: cell1-gnd -> cell1-gnd-1
- C36 pad 2: cell1-gnd -> cell1-gnd-1
- C37 pad 2: cell1-gnd -> cell1-gnd-1
- C38 pad 2: cell1-gnd -> cell1-gnd-1
- C41 pad 2: cell1-gnd -> cell1-gnd-1
- C42 pad 2: cell1-gnd -> cell1-gnd-1
- C54 pad 1: cell3-vcc -> cell3-gnd-1
- L3 pad 2: cell1-gnd -> cell1-gnd-1
- L7 pad 2: cell3-vcc -> cell3-gnd-1
- LED3 pad 2: cell1-vcc-1 -> vcc-2
- LED6 pad 2: cell2-vcc-1 -> vcc-2
- LED9 pad 2: cell3-vcc-1 -> vcc-2
- Q4 pad 2: cell1-gnd -> cell1-gnd-1
- Q5 pad 2: cell1-gnd -> gnd
- Q8 pad 2: cell2-gnd-1 -> gnd
- R100 pad 1: cell3-vcc-2 -> cell3-sda
- R100 pad 2: cell3_debug_2.header-_7 -> cell3-vcc-2
- R29 pad 2: io0 -> io15
- R40 pad 1: cell1-gnd -> cell1-gnd-1
- R40 pad 2: cell1.current_sense.sensor-vcc -> cell1.adc-vcc-2
- R45 pad 1: cell1.dmm_relay-input -> io1
- R46 pad 1: cell1.dmm_relay-input -> io1
- R56 pad 2: cell1-gnd -> cell1-gnd-1
- R59 pad 2: cell1-gnd -> cell1-gnd-1
- R63 pad 2: cell1-gnd -> cell1-gnd-1
- R65 pad 2: cell2.current_sense.sensor-vcc -> cell2.adc-vcc-2
- R68 pad 2: cell1-gnd -> cell1-gnd-1
- R70 pad 1: cell2.dmm_relay-input -> io2
- R71 pad 1: cell2.dmm_relay-input -> io2
- R71 pad 2: cell1-gnd -> gnd
- R78 pad 2: cell1-gnd -> cell1-gnd-1
- R90 pad 1: cell3-vcc -> cell3-gnd-1
- R90 pad 2: cell3.current_sense.sensor-vcc -> cell3.adc-vcc-2
- R95 pad 1: cell3.dmm_relay-input -> io3
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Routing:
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- added copper zone on B.Cu, net cell1-gnd-1
- added copper zone on F.Cu, net cell1-gnd-1
- added copper zone on In2.Cu, net cell1-gnd-1
- added copper zone on F.Cu, net cell2-gnd-1
- added copper zone on B.Cu, net cell3-gnd-1
- added copper zone on F.Cu, net cell3-gnd-1
- added copper zone on In2.Cu, net cell3-gnd-1
- added copper zone on B.Cu, net cell4-gnd-1
- added copper zone on F.Cu, net cell4-gnd-1
- added copper zone on In2.Cu, net cell4-gnd-1
- added copper zone on In1.Cu, net cell4-vcc-2
- added copper zone on B.Cu, net cell5-gnd-1
- added copper zone on F.Cu, net cell5-gnd-1
- added copper zone on In2.Cu, net cell5-gnd-1
- added copper zone on In1.Cu, net cell5-vcc-2
- added copper zone on B.Cu, net cell6-gnd-1
- added copper zone on F.Cu, net cell6-gnd-1
- added copper zone on In2.Cu, net cell6-gnd-1
- added copper zone on In1.Cu, net cell6-vcc-2
- added copper zone on In1.Cu, net cell7-vcc-3
- removed copper zone on B.Cu, net cell1-gnd
- removed copper zone on In2.Cu, net cell1-gnd
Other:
- board outline removed
- board text added: "CellN"
- board text removed: "Cell1"
- board text removed: "Cell2"
- board text removed: "Cell3"
- board text removed: "Cell3 Voltage Domain!!!"
- board text removed: "I Out DMM 5V"
- board text removed: "Narayan"
- board text removed: "SCL SDA BUCK LDO"
